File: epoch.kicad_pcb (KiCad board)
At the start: 4 copper layers, 28 x 34 mm, 34 parts, among them J1 USB_OTG, J2 CONN_01X05, J3 CONN_01X02, P3 CONN_01X10, SW1 SW_Reset, U1 MIC5219-3.3BM5, U2 ATSAMD21Ennc-AU, U3 DS3231MZ, U4 MCP7940N-I/SN, U5 74HC1G14GW, U6 MH2mm, U7 MH2mm, U8 MH2mm, U9 MH2mm

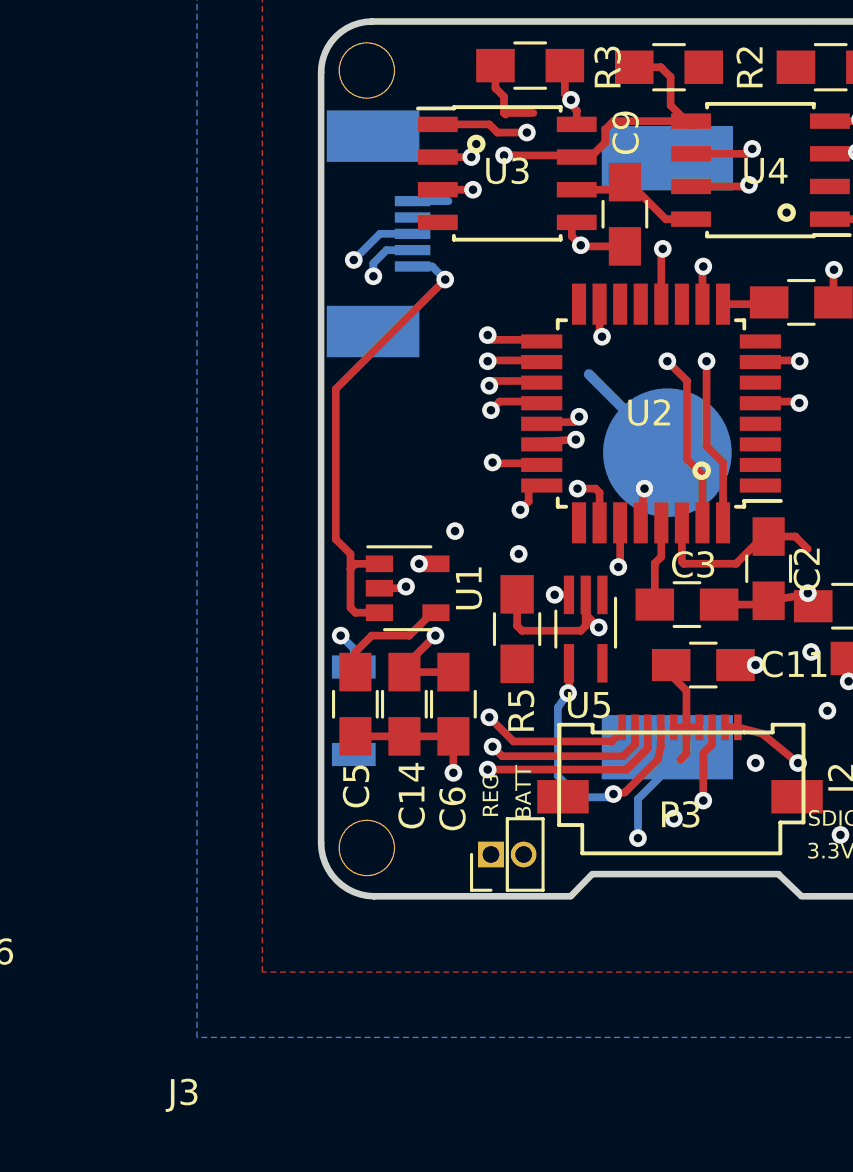
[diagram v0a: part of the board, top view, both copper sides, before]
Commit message: Remove connector and redo the connections
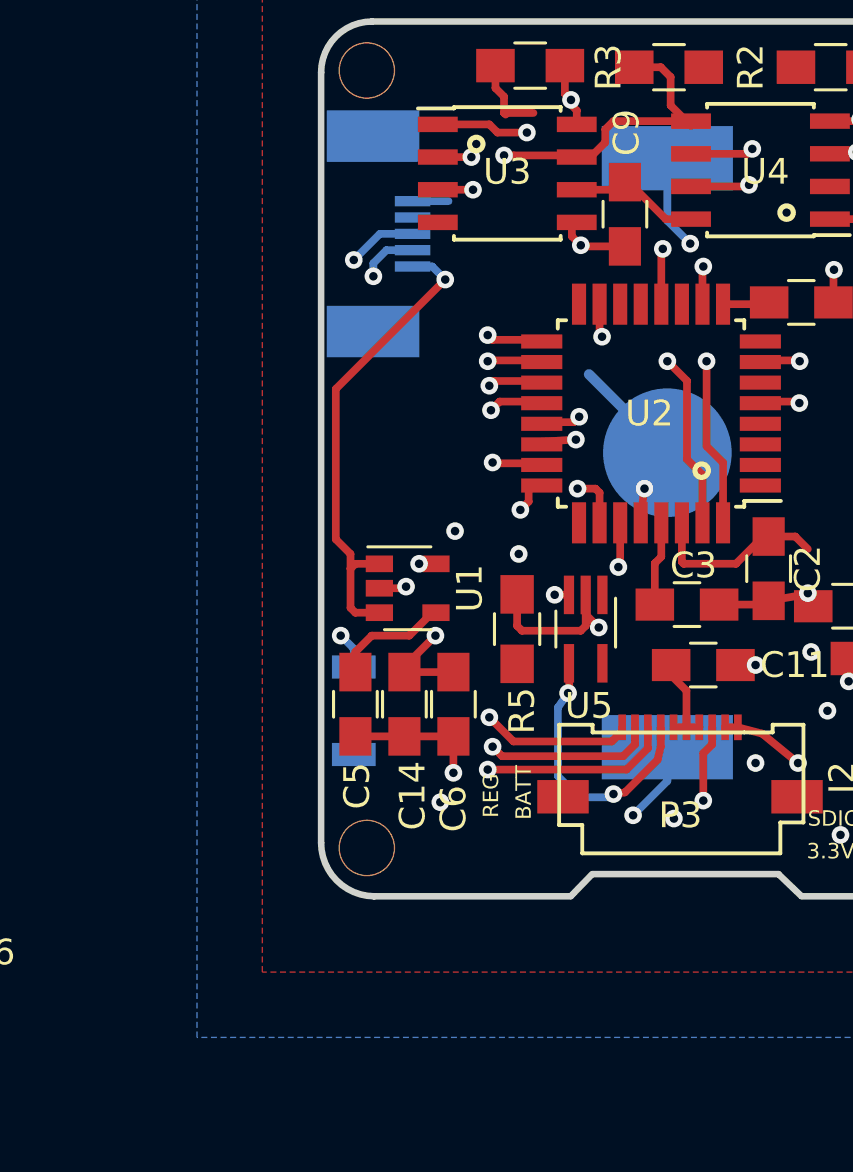
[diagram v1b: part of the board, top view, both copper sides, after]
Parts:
- removed J3: CONN_01X02, Pin_Headers:Pin_Header_Straight_1x02_Pitch1.27mm
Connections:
- BT1 pad 1: +3.3V(BATT) -> (+3.3)
- C14 pad 1: +3.3V(REGUL) -> (+3.3)
- C6 pad 1: +3.3V(REGUL) -> (+3.3)
- U1 pad 5: +3.3V(REGUL) -> (+3.3)
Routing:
- net (+3.3): track 22.4 -> 43.9 mm, vias 0 -> 5
- net +3.3V(REGUL): track 18.8 -> 0.00 mm, vias 2 -> 0
- net +3.3V(BATT): track 8.72 -> 0.00 mm, vias 1 -> 0

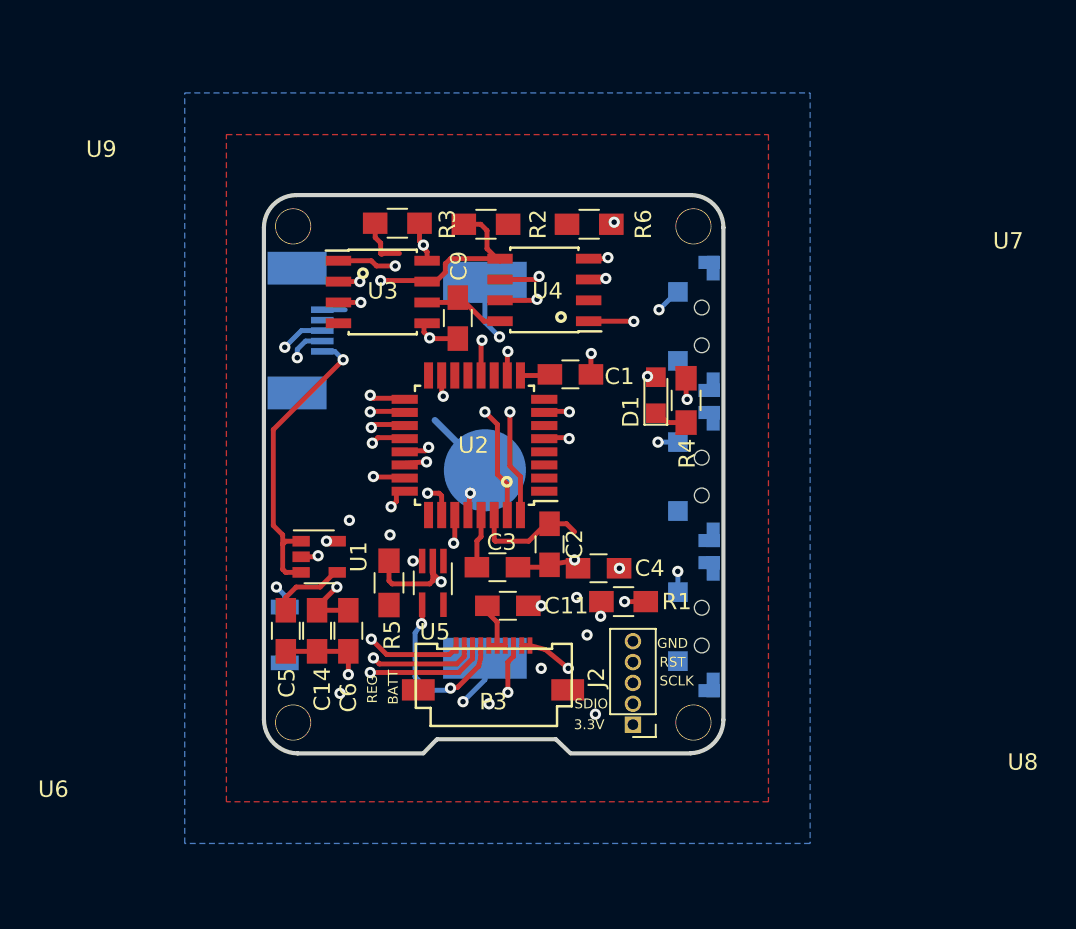
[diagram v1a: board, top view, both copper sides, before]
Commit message: Update for LIPO power_board
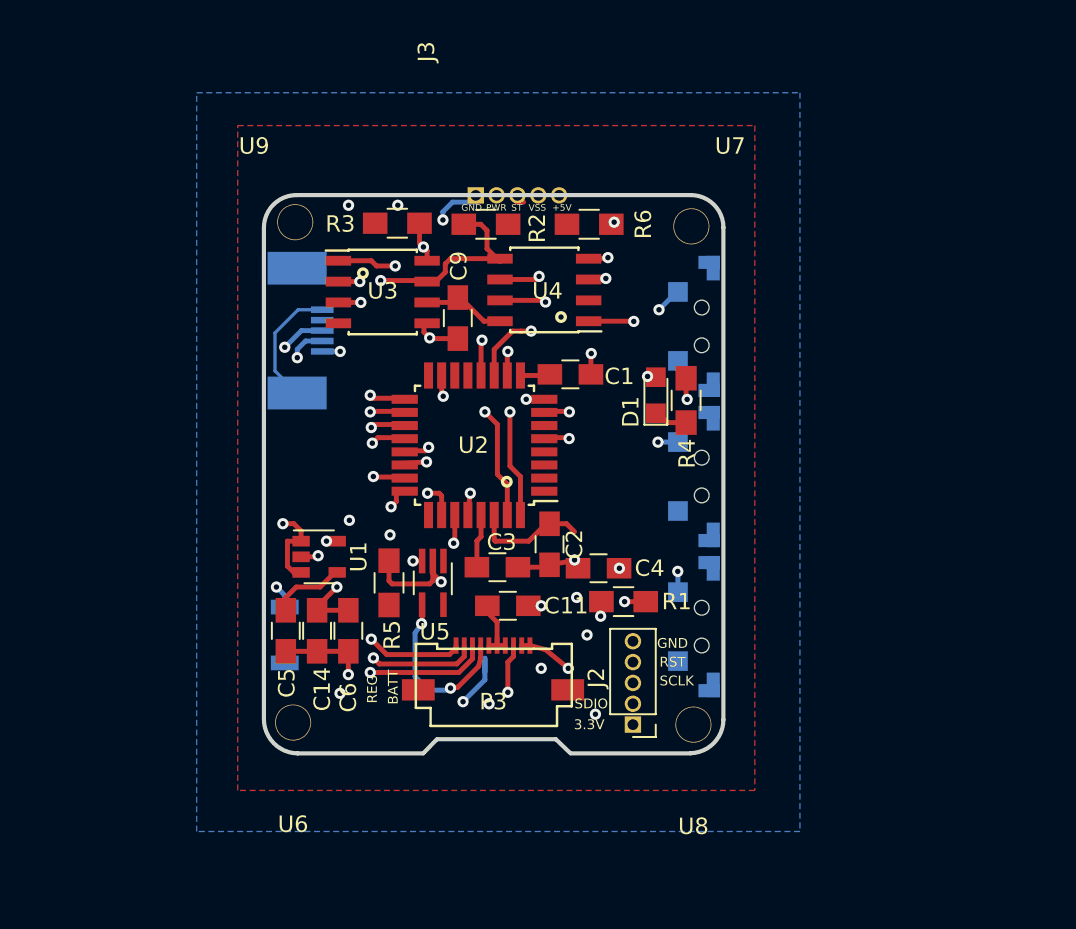
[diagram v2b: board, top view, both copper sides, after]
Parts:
- removed BT1: Battery_Cell, Connectors:CR2032-001
- added J3: CONN_01X05, my-fp-library:Pin_Header_Straight_1x05_Pitch1.27mm_no_silk, F.Cu at (114.2, 54.5)
- U6, U7, U8, U9: footprint my-fp-library:MH2mm -> my-fp-library:MH2.1mm
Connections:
- J1 pad 1: VCC -> VSS
- U1 pad 1: VCC -> (+5)
- U1 pad 3: VCC -> (+5)
- U2 pad 11: (no net) -> STAT
- U2 pad 8: (no net) -> PWR_SENSE
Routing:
- net (+5): track 0.00 -> 40.9 mm, vias 0 -> 2
- net VSS: track 0.00 -> 27.3 mm, vias 0 -> 2
- net VCC: track 18.6 -> 0.00 mm, vias 1 -> 0
- net PWR_SENSE: track 0.00 -> 14.1 mm, vias 0 -> 1
- net STAT: track 0.00 -> 14.0 mm, vias 0 -> 1
- net (+3.3): track 43.9 -> 37.0 mm, vias 5 -> 4
- net (GND): track 35.5 -> 37.6 mm, vias 14 -> 15
- net 32KHz: track 29.5 -> 28.9 mm
- net SCL: track 34.2 -> 33.6 mm
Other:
- board text added: "+5V"
- board text added: "PWR"
- board text added: "ST"
- board text added: "VSS"

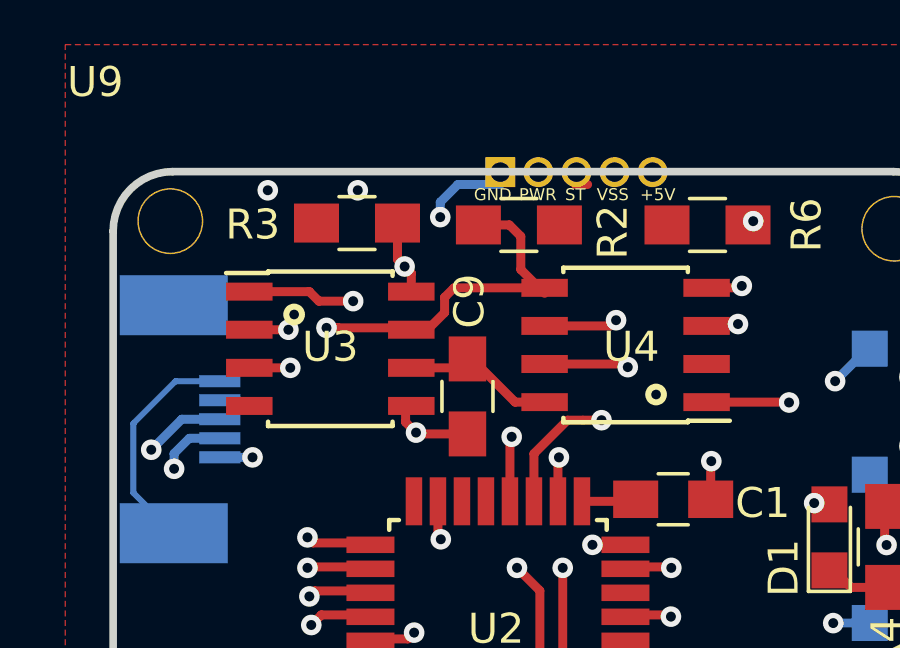
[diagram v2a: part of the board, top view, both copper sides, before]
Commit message: New connections to power board
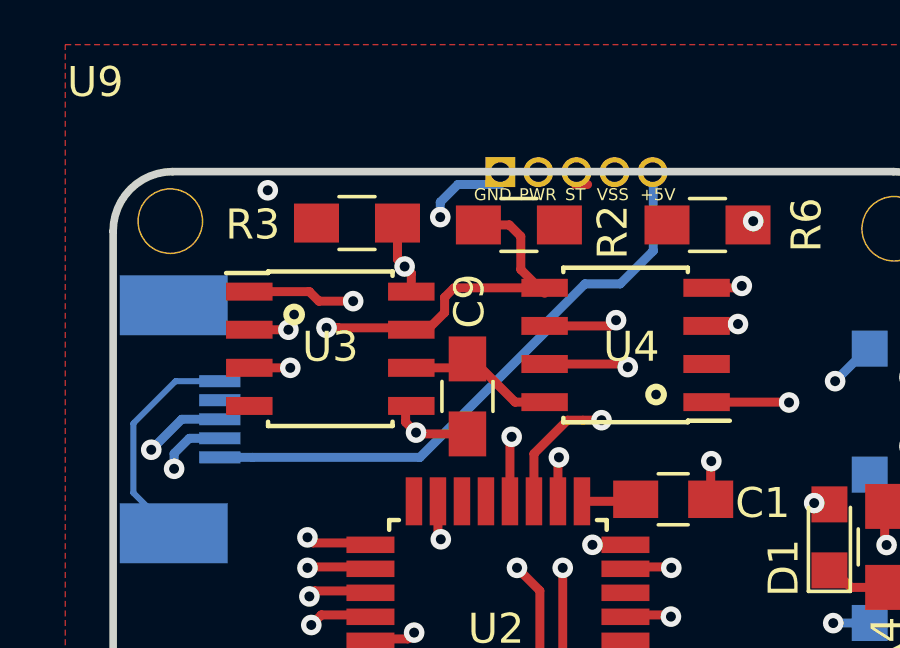
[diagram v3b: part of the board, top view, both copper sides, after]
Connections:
- J1 pad 1: VSS -> VDD
- J3 pad 4: VSS -> (+5)
- J3 pad 5: (+5) -> VDD
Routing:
- net VSS: track 27.3 -> 0.00 mm, vias 2 -> 0
- net VDD: track 0.00 -> 19.7 mm
- net (+5): track 40.9 -> 40.2 mm
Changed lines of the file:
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@@
     (thickness 1.6002)
     (drawings 27)
-    (tracks 477)
+    (tracks 472)
     (zones 0)
     (modules 33)
@@
   )
   (setup
-    (last_trace_width 0.1524)
+    (last_trace_width 0.3)
     (user_trace_width 0.1524)
     (user_trace_width 0.2)
@@
   (net 25 SWDCLK)
   (net 26 "(+5)")
-  (net 27 VSS)
-  (net 28 PWR_SENSE)
-  (net 29 STAT)
+  (net 27 PWR_SENSE)
+  (net 28 STAT)
+  (net 29 VDD)
   (net_class Default "This is the default net class."
     (clearance 0.1524)
@@
     (add_net USB_D-)
     (add_net VCOM)
-    (add_net VSS)
+    (add_net VDD)
   )
   (module TO_SOT_Packages_SMD:SOT-23-5 (layer F.Cu)
@@
       (net 6 USB_D+))
     (pad 1 smd rect (at -1.27 0.635 90) (size 0.4 1.38) (layers B.Cu B.Paste B.Mask)
-      (net 27 VSS))
+      (net 29 VDD))
     (pad 6 smd rect (at 3.8 -0.9 90) (size 2 3.6) (layers B.Cu B.Paste B.Mask)
       (net 2 "(GND)"))
@@
       (net 21 LED))
     (pad 8 smd rect (at -4.25 2.8 180) (size 1.6 0.55) (layers F.Cu F.Paste F.Mask)
-      (net 28 PWR_SENSE))
+      (net 27 PWR_SENSE))
     (pad 9 smd rect (at -2.8 4.25 270) (size 1.6 0.55) (layers F.Cu F.Paste F.Mask)
       (net 1 "(+3.3)"))
@@
       (net 2 "(GND)"))
     (pad 11 smd rect (at -1.2 4.25 270) (size 1.6 0.55) (layers F.Cu F.Paste F.Mask)
-      (net 29 STAT))
+      (net 28 STAT))
     (pad 12 smd rect (at -0.4 4.25 270) (size 1.6 0.55) (layers F.Cu F.Paste F.Mask)
       (net 20 INTC))
@@
       (effects (font (size 1 1) (thickness 0.15)))
     )
-    (fp_text value CONN_01X05 (at 0 6.835 90) (layer F.Fab)
+    (fp_text value CONN_01X05 (at 6.275 25.1 90) (layer F.Fab)
       (effects (font (size 1 1) (thickness 0.15)))
     )
@@
     (fp_line (start -1.27 -0.635) (end -1.27 5.715) (layer F.Fab) (width 0.1))
     (pad 5 thru_hole oval (at 0 5.08 90) (size 1 1) (drill 0.65) (layers *.Cu *.Mask)
+      (net 29 VDD))
+    (pad 4 thru_hole oval (at 0 3.81 90) (size 1 1) (drill 0.65) (layers *.Cu *.Mask)
       (net 26 "(+5)"))
-    (pad 4 thru_hole oval (at 0 3.81 90) (size 1 1) (drill 0.65) (layers *.Cu *.Mask)
-      (net 27 VSS))
     (pad 3 thru_hole oval (at 0 2.54 90) (size 1 1) (drill 0.65) (layers *.Cu *.Mask)
-      (net 29 STAT))
+      (net 28 STAT))
     (pad 2 thru_hole oval (at 0 1.27 90) (size 1 1) (drill 0.65) (layers *.Cu *.Mask)
-      (net 28 PWR_SENSE))
+      (net 27 PWR_SENSE))
     (pad 1 thru_hole rect (at 0 0 90) (size 1 1) (drill 0.65) (layers *.Cu *.Mask)
       (net 2 "(GND)"))
@@
   (segment (start 101.970699 73.970699) (end 101.970699 59.634615) (width 0.3) (layer In1.Cu) (net 26))
   (segment (start 108.237585 56.842899) (end 106.842899 55.448213) (width 0.3) (layer In2.Cu) (net 26))
-  (segment (start 117.319511 56.842899) (end 108.237585 56.842899) (width 0.3) (layer In2.Cu) (net 26))
-  (segment (start 119.25 54.91241) (end 117.319511 56.842899) (width 0.3) (layer In2.Cu) (net 26))
   (segment (start 102.5 74.5) (end 101.970699 73.970699) (width 0.3) (layer In1.Cu) (net 26))
-  (segment (start 104.902 64.008) (end 105.992 64.008) (width 0.3) (layer B.Cu) (net 27))
-  (via (at 105.992 64.008) (size 0.6858) (drill 0.3302) (layers F.Cu B.Cu) (net 27))
-  (segment (start 105.992 64.008) (end 111.706801 58.293199) (width 0.3) (layer In1.Cu) (net 27))
-  (segment (start 111.706801 58.293199) (end 111.706801 57.221255) (width 0.3) (layer In1.Cu) (net 27))
-  (via (at 109.5 55.1053) (size 0.6858) (drill 0.3302) (layers F.Cu B.Cu) (net 27))
-  (segment (start 111.280399 56.885699) (end 109.5 55.1053) (width 0.3) (layer In1.Cu) (net 27))
-  (segment (start 111.371245 56.885699) (end 111.280399 56.885699) (width 0.3) (layer In1.Cu) (net 27))
-  (segment (start 109.5 55.014454) (end 111.371245 56.885699) (width 0.3) (layer In1.Cu) (net 27))
-  (segment (start 111.706801 57.221255) (end 109.5 55.1053) (width 0.3) (layer In1.Cu) (net 27))
-  (segment (start 117.197599 55.302401) (end 117.58759 54.91241) (width 0.3) (layer In2.Cu) (net 27))
-  (segment (start 110.182034 55.302401) (end 117.197599 55.302401) (width 0.3) (layer In2.Cu) (net 27))
-  (segment (start 109.5 55.1053) (end 109.984933 55.1053) (width 0.3) (layer In2.Cu) (net 27))
-  (segment (start 109.984933 55.1053) (end 110.182034 55.302401) (width 0.3) (layer In2.Cu) (net 27))
-  (segment (start 117.58759 54.91241) (end 118 54.91241) (width 0.3) (layer In2.Cu) (net 27))
-  (segment (start 118.423 66.923) (end 117.323 66.923) (width 0.3) (layer F.Cu) (net 28))
-  (via (at 117.323 66.923) (size 0.6858) (drill 0.3302) (layers F.Cu B.Cu) (net 28))
-  (segment (start 117.25 66.996) (end 117.323 66.923) (width 0.3) (layer F.Cu) (net 28))
-  (segment (start 116.980101 56.230101) (end 115.66241 54.91241) (width 0.3) (layer In1.Cu) (net 28))
-  (segment (start 117.323 66.923) (end 116.980101 66.580101) (width 0.3) (layer In1.Cu) (net 28))
-  (segment (start 116.980101 66.580101) (end 116.980101 56.230101) (width 0.3) (layer In1.Cu) (net 28))
-  (segment (start 115.66241 54.91241) (end 115.5 54.91241) (width 0.3) (layer In1.Cu) (net 28))
-  (segment (start 116.489053 62.768901) (end 117.002145 62.768901) (width 0.3) (layer F.Cu) (net 29))
-  (segment (start 115.373 65.473) (end 115.373 63.884954) (width 0.3) (layer F.Cu) (net 29))
-  (segment (start 115.373 63.884954) (end 116.489053 62.768901) (width 0.3) (layer F.Cu) (net 29))
-  (segment (start 117.16241 54.91241) (end 116.75 54.91241) (width 0.3) (layer F.Cu) (net 29))
-  (via (at 117.625401 62.768901) (size 0.6858) (drill 0.3302) (layers F.Cu B.Cu) (net 29))
-  (segment (start 117.002145 62.768901) (end 117.625401 62.768901) (width 0.3) (layer F.Cu) (net 29))
-  (segment (start 118.755301 56.755301) (end 116.91241 54.91241) (width 0.3) (layer In1.Cu) (net 29))
-  (segment (start 118.755301 59.745745) (end 118.755301 56.755301) (width 0.3) (layer In1.Cu) (net 29))
-  (segment (start 117.625401 62.768901) (end 117.625401 60.875645) (width 0.3) (layer In1.Cu) (net 29))
-  (segment (start 117.625401 60.875645) (end 118.755301 59.745745) (width 0.3) (layer In1.Cu) (net 29))
-  (segment (start 116.91241 54.91241) (end 116.75 54.91241) (width 0.3) (layer In1.Cu) (net 29))
+  (segment (start 108.237585 56.842899) (end 117.007101 56.842899) (width 0.3) (layer In2.Cu) (net 26))
+  (segment (start 117.007101 56.842899) (end 118.05 55.8) (width 0.3) (layer In2.Cu) (net 26))
+  (segment (start 118.05 55.8) (end 118.05 54.91241) (width 0.3) (layer In2.Cu) (net 26))
+  (segment (start 104.902 64.008) (end 105.992 64.008) (width 0.3) (layer B.Cu) (net 29))
+  (segment (start 118.423 66.923) (end 117.323 66.923) (width 0.3) (layer F.Cu) (net 27))
+  (via (at 117.323 66.923) (size 0.6858) (drill 0.3302) (layers F.Cu B.Cu) (net 27))
+  (segment (start 117.25 66.996) (end 117.323 66.923) (width 0.3) (layer F.Cu) (net 27))
+  (segment (start 116.980101 56.230101) (end 115.66241 54.91241) (width 0.3) (layer In1.Cu) (net 27))
+  (segment (start 117.323 66.923) (end 116.980101 66.580101) (width 0.3) (layer In1.Cu) (net 27))
+  (segment (start 116.980101 66.580101) (end 116.980101 56.230101) (width 0.3) (layer In1.Cu) (net 27))
+  (segment (start 115.66241 54.91241) (end 115.5 54.91241) (width 0.3) (layer In1.Cu) (net 27))
+  (segment (start 116.489053 62.768901) (end 117.002145 62.768901) (width 0.3) (layer F.Cu) (net 28))
+  (segment (start 115.373 65.473) (end 115.373 63.884954) (width 0.3) (layer F.Cu) (net 28))
+  (segment (start 115.373 63.884954) (end 116.489053 62.768901) (width 0.3) (layer F.Cu) (net 28))
+  (segment (start 117.16241 54.91241) (end 116.75 54.91241) (width 0.3) (layer F.Cu) (net 28))
+  (via (at 117.625401 62.768901) (size 0.6858) (drill 0.3302) (layers F.Cu B.Cu) (net 28))
+  (segment (start 117.002145 62.768901) (end 117.625401 62.768901) (width 0.3) (layer F.Cu) (net 28))
+  (segment (start 118.755301 56.755301) (end 116.91241 54.91241) (width 0.3) (layer In1.Cu) (net 28))
+  (segment (start 118.755301 59.745745) (end 118.755301 56.755301) (width 0.3) (layer In1.Cu) (net 28))
+  (segment (start 117.625401 62.768901) (end 117.625401 60.875645) (width 0.3) (layer In1.Cu) (net 28))
+  (segment (start 117.625401 60.875645) (end 118.755301 59.745745) (width 0.3) (layer In1.Cu) (net 28))
+  (segment (start 116.91241 54.91241) (end 116.75 54.91241) (width 0.3) (layer In1.Cu) (net 28))
+  (segment (start 111.572046 64.008) (end 115.8 59.780046) (width 0.3) (layer B.Cu) (net 29))
+  (segment (start 105.992 64.008) (end 111.572046 64.008) (width 0.3) (layer B.Cu) (net 29))
+  (segment (start 115.8 59.780046) (end 115.8 59.5) (width 0.3) (layer B.Cu) (net 29))
+  (segment (start 115.8 59.5) (end 117.075 58.225) (width 0.3) (layer B.Cu) (net 29))
+  (segment (start 117.075 58.225) (end 118.25 58.225) (width 0.3) (layer B.Cu) (net 29))
+  (segment (start 118.25 58.225) (end 119.35 57.125) (width 0.3) (layer B.Cu) (net 29))
+  (segment (start 119.35 57.125) (end 119.35 54.91241) (width 0.3) (layer B.Cu) (net 29))
   (zone (net 2) (net_name "(GND)") (layer B.Cu) (hatch edge 0.508)
     (connect_pads (clearance 0.508))
